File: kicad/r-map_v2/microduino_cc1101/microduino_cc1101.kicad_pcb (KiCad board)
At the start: 2 copper layers, 3 parts, among them J1 Conn_Coaxial, U1 Microduino, U2 CC1101-868MHz-Module

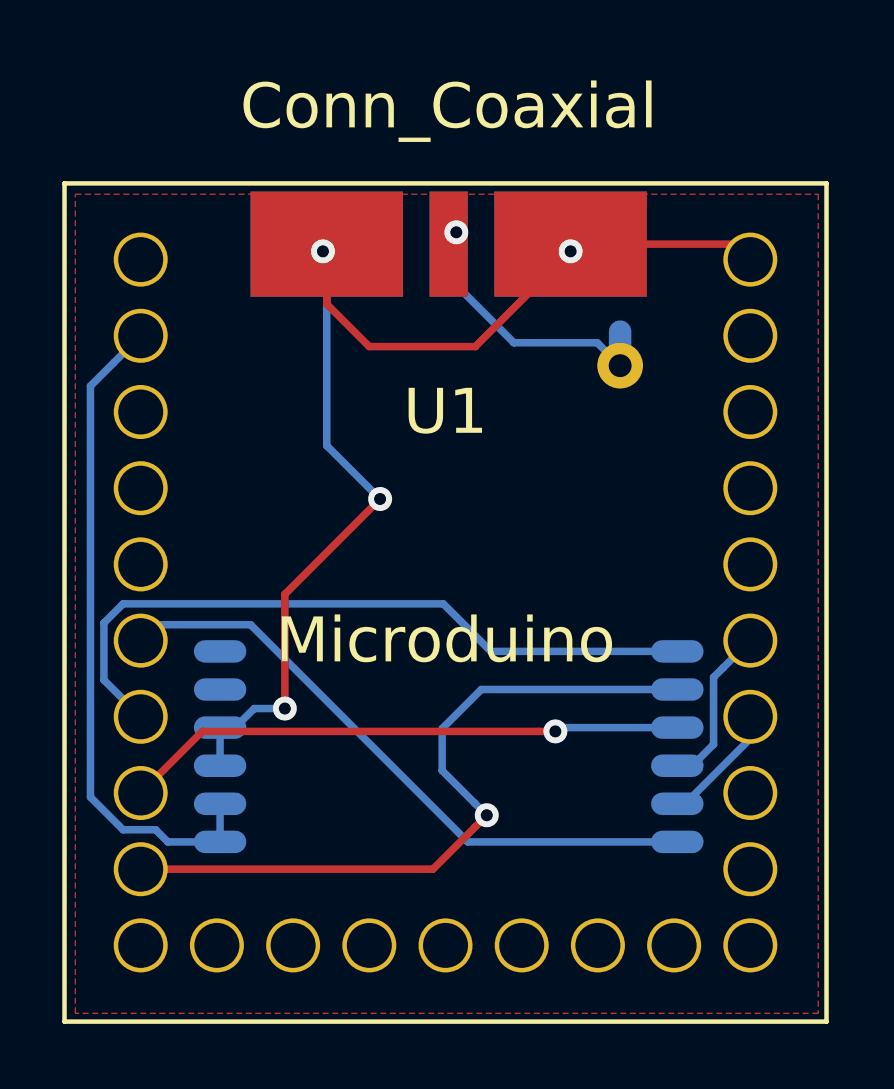
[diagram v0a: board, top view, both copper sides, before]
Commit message: Update of project with updated microduino module
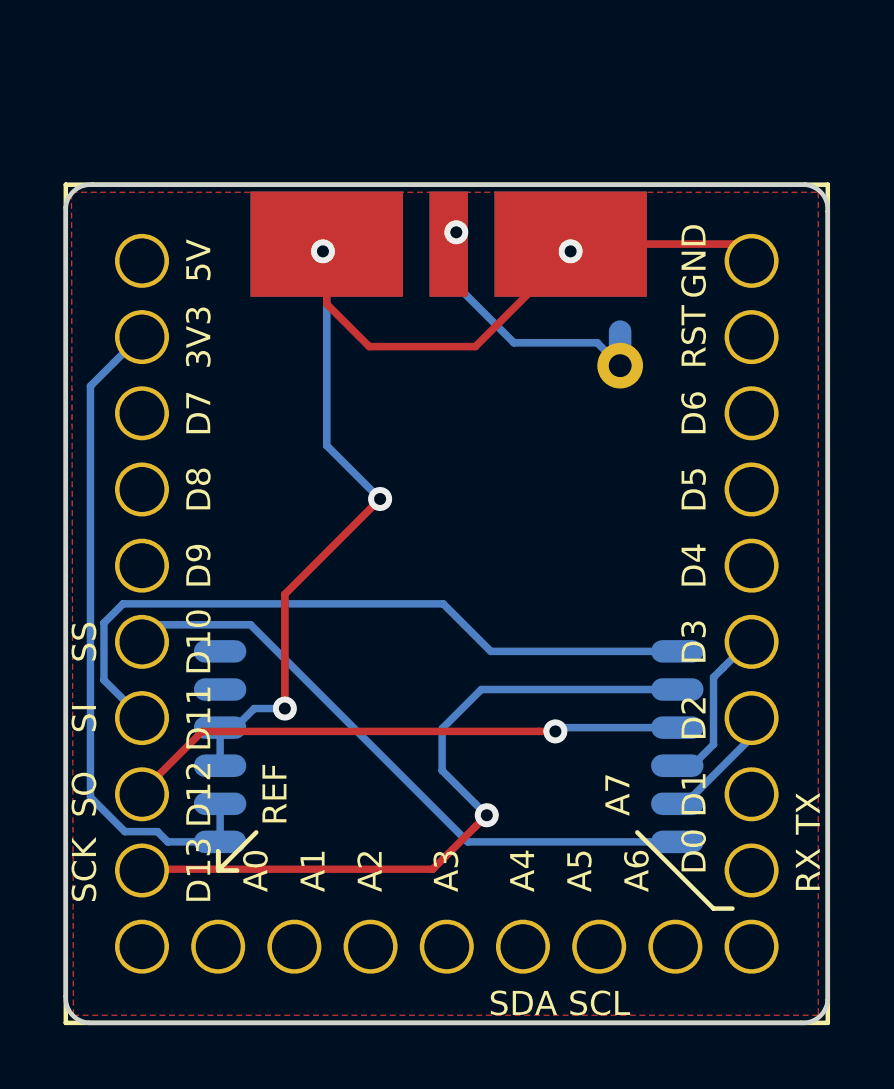
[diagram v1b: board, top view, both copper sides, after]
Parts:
- moved U1 0.06 mm to (136.8, 60.0)
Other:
- board outline added: 25.4 x 27.9 mm

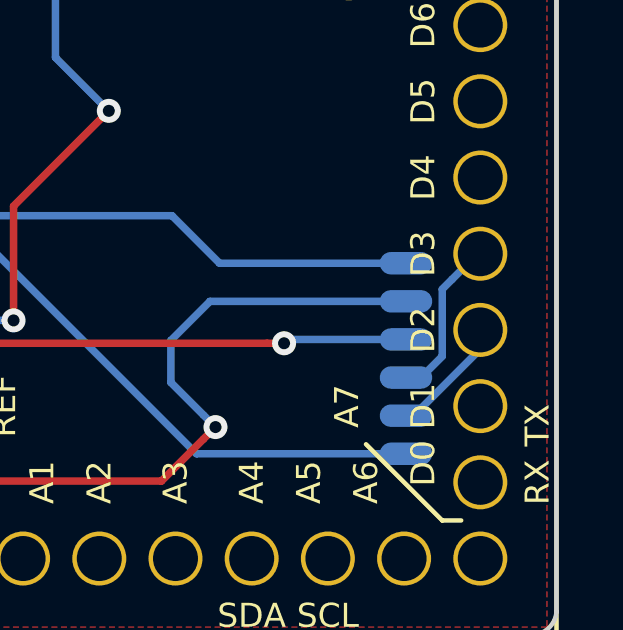
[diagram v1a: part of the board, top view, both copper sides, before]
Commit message: Remove unwanted connection for GD02
Unnecessary net remove from schematic and pcb
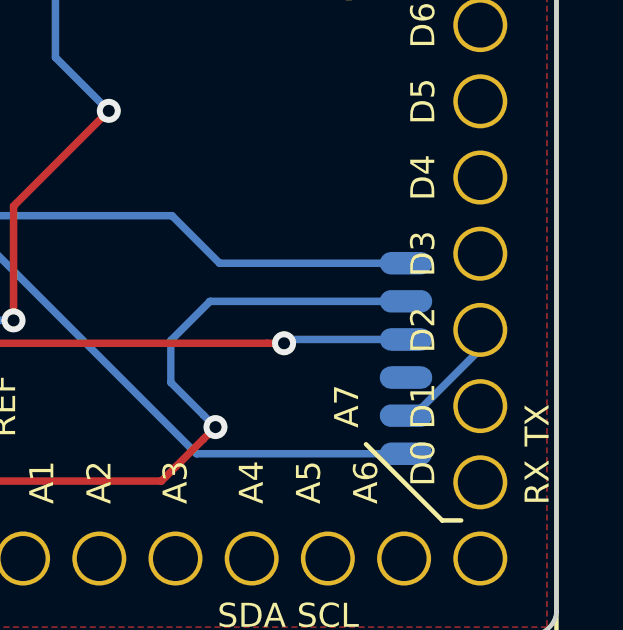
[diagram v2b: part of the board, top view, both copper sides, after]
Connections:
- U1 pad 10: Net-(U1-Pad10) -> (no net)
- U1 pad 11: Net-(U1-Pad11) -> (no net)
- U1 pad 12: Net-(U1-Pad12) -> (no net)
- U1 pad 13: Net-(U1-Pad13) -> (no net)
- U1 pad 14: Net-(U1-Pad14) -> (no net)
- U1 pad 15: Net-(U1-Pad15) -> (no net)
- U1 pad 16: Net-(U1-Pad16) -> (no net)
- U1 pad 17: Net-(U1-Pad17) -> (no net)
- U1 pad 18: Net-(U1-Pad18) -> (no net)
- U1 pad 23: Net-(U1-Pad23) -> (no net)
- U1 pad 24: Net-(U1-Pad24) -> (no net)
- U1 pad 25: Net-(U1-Pad25) -> (no net)
- U1 pad 27: Net-(U1-Pad27) -> (no net)
- U1 pad 6: GD01 -> Net-(U1-Pad6)
- U2 pad 4: GD01 -> Net-(U2-Pad4)
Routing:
- net GD01: track 5.47 -> 0.00 mm
- net Net-(U2-Pad4): track 0.00 -> 0.50 mm
